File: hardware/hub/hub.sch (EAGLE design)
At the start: 22 parts, among them IC1 7805TV, IC2 LM3940, J1 AVR_SPI_PRG_6PTH, J2 POWER_JACKPTH, U1 ATMEGA328P_PDIP, U2 ENC28J60, U3 NRF24L01+

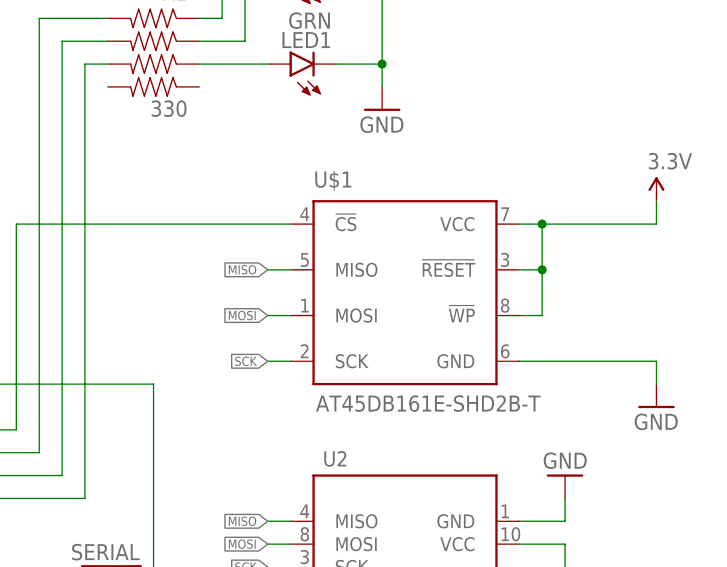
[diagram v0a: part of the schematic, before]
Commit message: Fix flash pinout. Finish hub brd
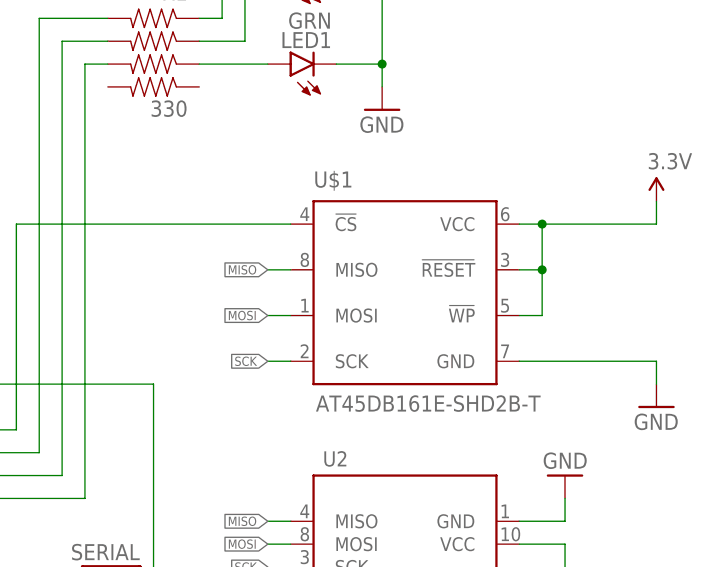
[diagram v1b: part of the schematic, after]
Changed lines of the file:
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@@
 <?xml version="1.0" encoding="utf-8"?>
 <!DOCTYPE eagle SYSTEM "eagle.dtd">
-<eagle version="6.5.0">
+<eagle version="6.6.0">
 <drawing>
 <settings>
